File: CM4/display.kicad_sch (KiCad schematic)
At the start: 1 part, among them U10 4inch_RPi_LCD_(C)

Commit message: Started the "fun" of routing
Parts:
- U10: footprint Connector_PinSocket_2.54mm:PinSocket_2x13_P2.54mm_Vertical -> (none)
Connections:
- net +3.3 High Current: now also U10.17 (3.3V)
- net +5: now also U10.4 (5V)
- net GND: now also U10.14 (GND), U10.20 (GND), U10.25 (GND), U10.9 (GND)
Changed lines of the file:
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@@
 (kicad_sch (version 20210126) (generator eeschema)
   (paper "A4")
+  (wire (pts (xy 97.79 107.95) (xy 97.79 110.49))
+    (stroke (width 0) (type solid) (color 0 0 0 0))
+  )
+  (wire (pts (xy 97.79 113.03) (xy 97.79 114.935))
+    (stroke (width 0) (type solid) (color 0 0 0 0))
+  )
   (global_label "TP_CS" (shape input) (at 97.79 87.63 0)
     (effects (font (size 1.27 1.27)) (justify left))
@@
     )
   )
-  (global_label "+5" (shape input) (at 97.79 110.49 0)
+  (global_label "+3.3 High Current" (shape input) (at 97.79 107.95 0)
     (effects (font (size 1.27 1.27)) (justify left))
-    (property "Intersheet References" "${INTERSHEET_REFS}" (id 0) (at 102.985 110.4106 0)
+    (property "Intersheet References" "${INTERSHEET_REFS}" (id 0) (at 117.9226 107.8706 0)
       (effects (font (size 1.27 1.27)) (justify left) hide)
     )
   )
-  (global_label "+3.3 High Current" (shape input) (at 97.79 113.03 0)
+  (global_label "+5" (shape input) (at 97.79 113.03 0)
     (effects (font (size 1.27 1.27)) (justify left))
-    (property "Intersheet References" "${INTERSHEET_REFS}" (id 0) (at 117.9226 112.9506 0)
+    (property "Intersheet References" "${INTERSHEET_REFS}" (id 0) (at 102.985 112.9506 0)
       (effects (font (size 1.27 1.27)) (justify left) hide)
     )
   )
-  (symbol (lib_id "power:GND") (at 97.79 107.95 90) (unit 1)
+  (symbol (lib_id "power:GND") (at 78.74 121.285 0) (unit 1)
     (in_bom yes) (on_board yes)
-    (property "Reference" "#PWR0148" (id 0) (at 104.14 107.95 0)
+    (property "Reference" "#PWR0152" (id 0) (at 78.74 127.635 0)
       (effects (font (size 1.27 1.27)) hide)
     )
-    (property "Value" "GND" (id 1) (at 100.9651 108.3385 90)
+    (property "Value" "GND" (id 1) (at 78.3515 124.4601 90)
       (effects (font (size 1.27 1.27)) (justify right))
     )
-    (property "Footprint" "" (id 2) (at 97.79 107.95 0)
+    (property "Footprint" "" (id 2) (at 78.74 121.285 0)
       (effects (font (size 1.27 1.27)) hide)
     )
-    (property "Datasheet" "" (id 3) (at 97.79 107.95 0)
+    (property "Datasheet" "" (id 3) (at 78.74 121.285 0)
       (effects (font (size 1.27 1.27)) hide)
     )
     (pin "1")
   )
-  (symbol (lib_id "teensy:4inch_RPi_LCD_(C)") (at 85.725 101.6 0) (unit 1)
+  (symbol (lib_id "power:GND") (at 81.28 121.285 0) (unit 1)
     (in_bom yes) (on_board yes)
-    (property "Reference" "U10" (id 0) (at 86.5124 79.1676 0))
-    (property "Value" "4inch_RPi_LCD_(C)" (id 1) (at 86.5124 81.4663 0))
-    (property "Footprint" "Connector_PinSocket_2.54mm:PinSocket_2x13_P2.54mm_Vertical" (id 2) (at 85.09 45.085 0)
+    (property "Reference" "#PWR0151" (id 0) (at 81.28 127.635 0)
       (effects (font (size 1.27 1.27)) hide)
     )
-    (property "Datasheet" "" (id 3) (at 85.09 45.085 0)
+    (property "Value" "GND" (id 1) (at 80.8915 124.4601 90)
+      (effects (font (size 1.27 1.27)) (justify right))
+    )
+    (property "Footprint" "" (id 2) (at 81.28 121.285 0)
+      (effects (font (size 1.27 1.27)) hide)
+    )
+    (property "Datasheet" "" (id 3) (at 81.28 121.285 0)
       (effects (font (size 1.27 1.27)) hide)
     )
     (pin "1")
+  )
+  (symbol (lib_id "power:GND") (at 83.82 121.285 0) (unit 1)
+    (in_bom yes) (on_board yes)
+    (property "Reference" "#PWR0150" (id 0) (at 83.82 127.635 0)
+      (effects (font (size 1.27 1.27)) hide)
+    )
+    (property "Value" "GND" (id 1) (at 83.4315 124.4601 90)
+      (effects (font (size 1.27 1.27)) (justify right))
+    )
+    (property "Footprint" "" (id 2) (at 83.82 121.285 0)
+      (effects (font (size 1.27 1.27)) hide)
+    )
+    (property "Datasheet" "" (id 3) (at 83.82 121.285 0)
+      (effects (font (size 1.27 1.27)) hide)
+    )
+    (pin "1")
+  )
+  (symbol (lib_id "power:GND") (at 86.36 121.285 0) (unit 1)
+    (in_bom yes) (on_board yes)
+    (property "Reference" "#PWR0149" (id 0) (at 86.36 127.635 0)
+      (effects (font (size 1.27 1.27)) hide)
+    )
+    (property "Value" "GND" (id 1) (at 85.9715 124.4601 90)
+      (effects (font (size 1.27 1.27)) (justify right))
+    )
+    (property "Footprint" "" (id 2) (at 86.36 121.285 0)
+      (effects (font (size 1.27 1.27)) hide)
+    )
+    (property "Datasheet" "" (id 3) (at 86.36 121.285 0)
+      (effects (font (size 1.27 1.27)) hide)
+    )
+    (pin "1")
+  )
+  (symbol (lib_id "power:GND") (at 88.9 121.285 0) (unit 1)
+    (in_bom yes) (on_board yes)
+    (property "Reference" "#PWR0148" (id 0) (at 88.9 127.635 0)
+      (effects (font (size 1.27 1.27)) hide)
+    )
+    (property "Value" "GND" (id 1) (at 88.5115 124.4601 90)
+      (effects (font (size 1.27 1.27)) (justify right))
+    )
+    (property "Footprint" "" (id 2) (at 88.9 121.285 0)
+      (effects (font (size 1.27 1.27)) hide)
+    )
+    (property "Datasheet" "" (id 3) (at 88.9 121.285 0)
+      (effects (font (size 1.27 1.27)) hide)
+    )
+    (pin "1")
+  )
+  (symbol (lib_id "teensy:4inch_RPi_LCD_(C)") (at 25.4 105.41 0) (unit 1)
+    (in_bom yes) (on_board yes)
+    (property "Reference" "U10" (id 0) (at 85.09 80.4376 0))
+    (property "Value" "4inch_RPi_LCD_(C)" (id 1) (at 85.09 82.7363 0))
+    (property "Footprint" "" (id 2) (at 24.765 48.895 0)
+      (effects (font (size 1.27 1.27)) hide)
+    )
+    (property "Datasheet" "" (id 3) (at 24.765 48.895 0)
+      (effects (font (size 1.27 1.27)) hide)
+    )
+    (pin "1")
+    (pin "10")
     (pin "11")
+    (pin "12")
+    (pin "13")
+    (pin "14")
+    (pin "15")
+    (pin "16")
+    (pin "17")
     (pin "18")
     (pin "19")
     (pin "2")
+    (pin "20")
     (pin "21")
     (pin "22")
     (pin "23")
     (pin "24")
+    (pin "25")
     (pin "26")
+    (pin "3")
+    (pin "4")
+    (pin "5")
     (pin "6")
+    (pin "7")
+    (pin "8")
+    (pin "9")
   )
 )

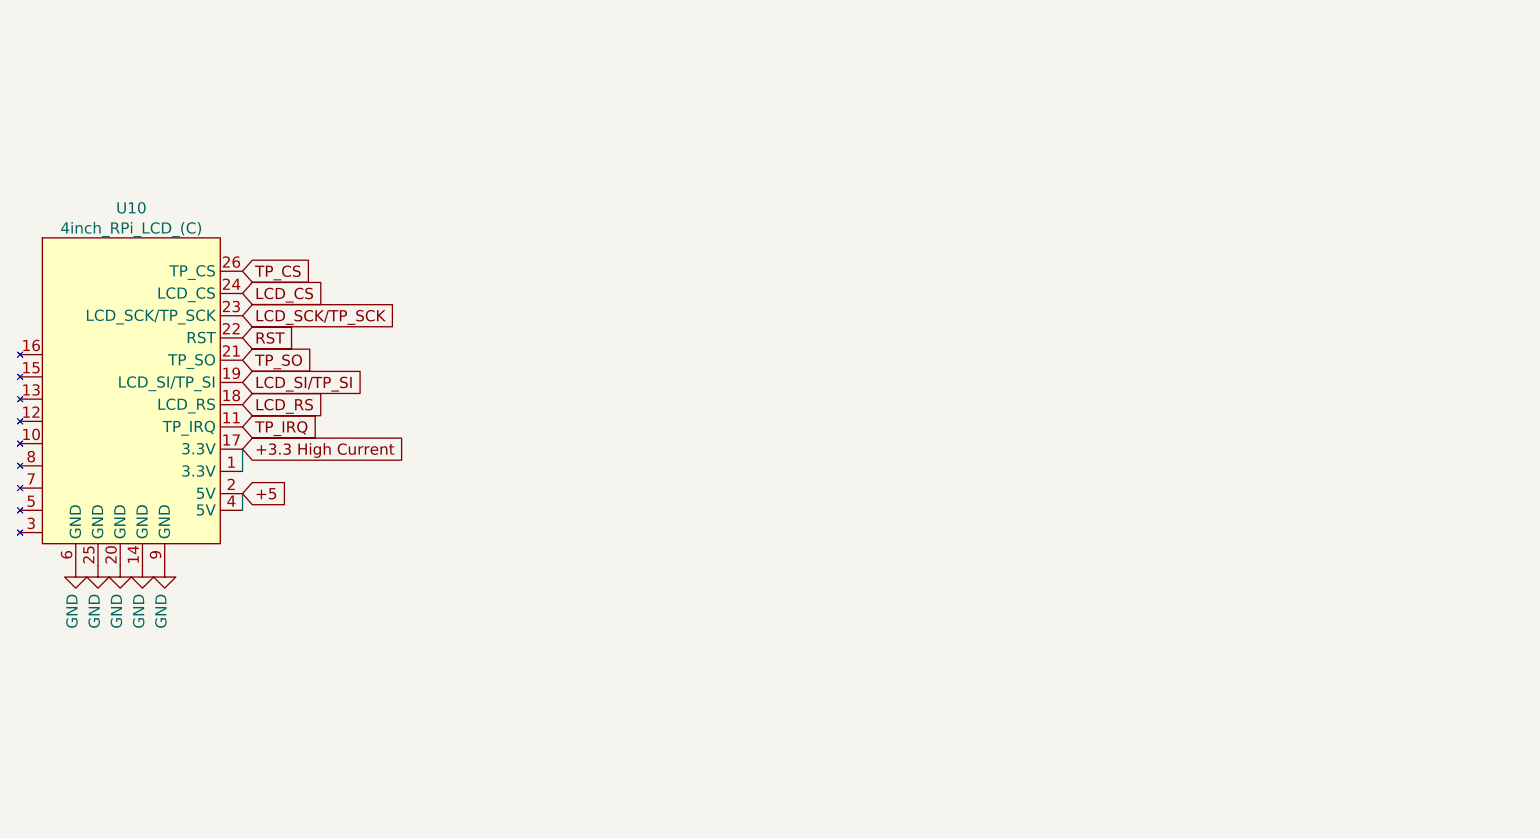
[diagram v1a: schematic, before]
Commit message: Bigone here we go
Whats gonna happon is im gonna get a 4 inch hdmi display and desolder the hdmi connector and add it to a ribbion cable and then add a connector to the pcb for hdmi to interface with that
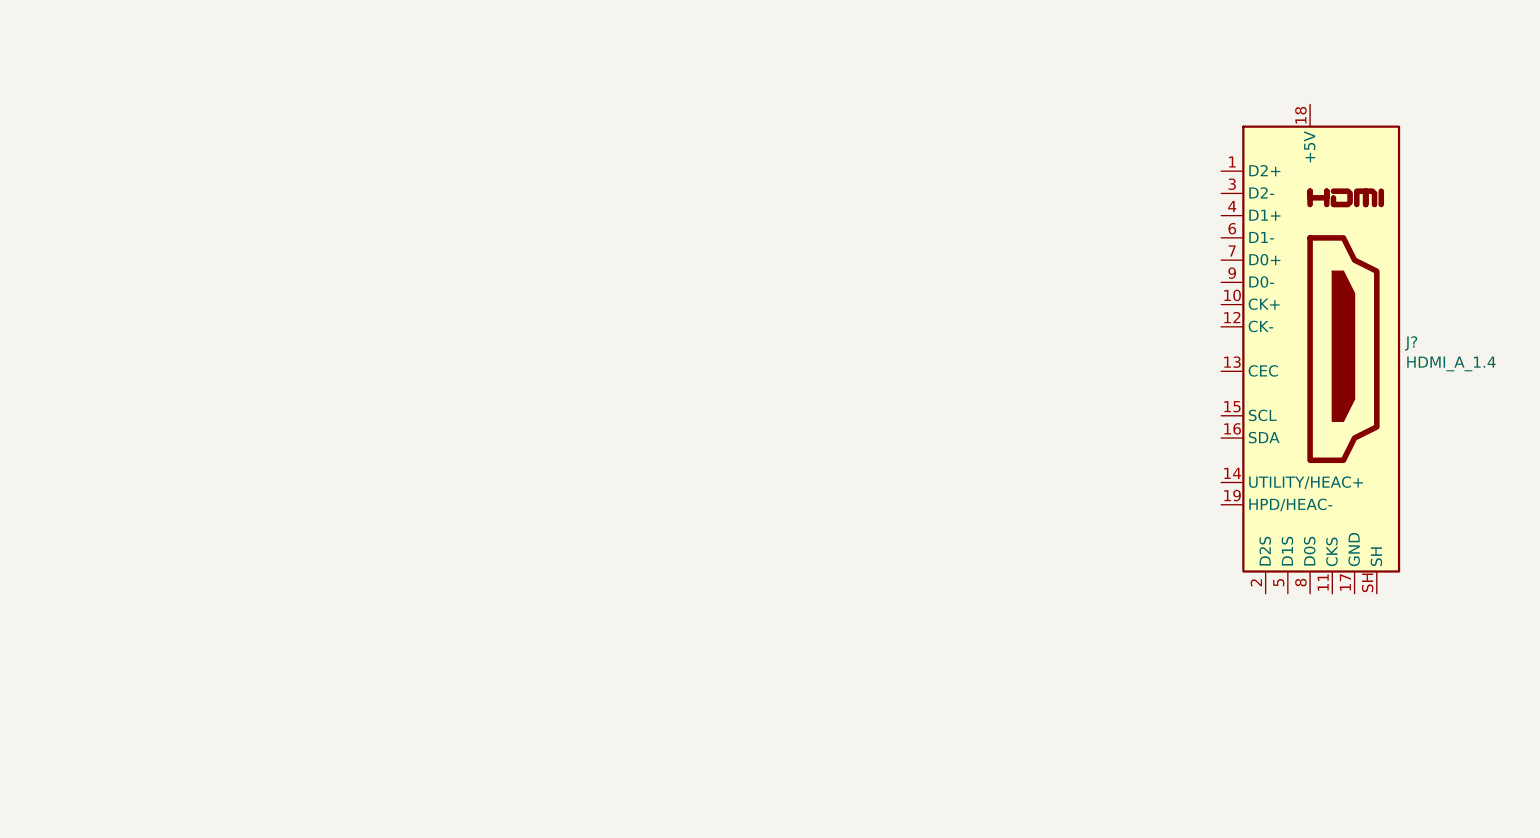
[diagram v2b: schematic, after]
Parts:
- removed U10: 4inch_RPi_LCD_(C), symbol teensy:4inch_RPi_LCD_(C)
- added J?: HDMI_A_1.4, symbol Connector:HDMI_A_1.4
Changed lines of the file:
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@@
 (kicad_sch (version 20210126) (generator eeschema)
   (paper "A4")
-  (wire (pts (xy 97.79 107.95) (xy 97.79 110.49))
-    (stroke (width 0) (type solid) (color 0 0 0 0))
-  )
-  (wire (pts (xy 97.79 113.03) (xy 97.79 114.935))
-    (stroke (width 0) (type solid) (color 0 0 0 0))
-  )
-  (global_label "TP_CS" (shape input) (at 97.79 87.63 0)
-    (effects (font (size 1.27 1.27)) (justify left))
-    (property "Intersheet References" "${INTERSHEET_REFS}" (id 0) (at 105.8879 87.5506 0)
-      (effects (font (size 1.27 1.27)) (justify left) hide)
+  (symbol (lib_id "Connector:HDMI_A_1.4") (at 219.71 96.52 0) (unit 1)
+    (in_bom yes) (on_board yes)
+    (property "Reference" "J?" (id 0) (at 230.6321 95.7591 0)
+      (effects (font (size 1.27 1.27)) (justify left))
     )
-  )
-  (global_label "LCD_CS" (shape input) (at 97.79 90.17 0)
-    (effects (font (size 1.27 1.27)) (justify left))
-    (property "Intersheet References" "${INTERSHEET_REFS}" (id 0) (at 107.2183 90.0906 0)
-      (effects (font (size 1.27 1.27)) (justify left) hide)
+    (property "Value" "HDMI_A_1.4" (id 1) (at 230.6321 98.0578 0)
+      (effects (font (size 1.27 1.27)) (justify left))
     )
-  )
-  (global_label "LCD_SCK{slash}TP_SCK" (shape input) (at 97.79 92.71 0)
-    (effects (font (size 1.27 1.27)) (justify left))
-    (property "Intersheet References" "${INTERSHEET_REFS}" (id 0) (at 116.7736 92.6306 0)
-      (effects (font (size 1.27 1.27)) (justify left) hide)
-    )
-  )
-  (global_label "RST" (shape input) (at 97.79 95.25 0)
-    (effects (font (size 1.27 1.27)) (justify left))
-    (property "Intersheet References" "${INTERSHEET_REFS}" (id 0) (at 103.6502 95.1706 0)
-      (effects (font (size 1.27 1.27)) (justify left) hide)
-    )
-  )
-  (global_label "TP_SO" (shape input) (at 97.79 97.79 0)
-    (effects (font (size 1.27 1.27)) (justify left))
-    (property "Intersheet References" "${INTERSHEET_REFS}" (id 0) (at 105.9483 97.7106 0)
-      (effects (font (size 1.27 1.27)) (justify left) hide)
-    )
-  )
-  (global_label "LCD_SI{slash}TP_SI" (shape input) (at 97.79 100.33 0)
-    (effects (font (size 1.27 1.27)) (justify left))
-    (property "Intersheet References" "${INTERSHEET_REFS}" (id 0) (at 112.9031 100.2506 0)
-      (effects (font (size 1.27 1.27)) (justify left) hide)
-    )
-  )
-  (global_label "LCD_RS" (shape input) (at 97.79 102.87 0)
-    (effects (font (size 1.27 1.27)) (justify left))
-    (property "Intersheet References" "${INTERSHEET_REFS}" (id 0) (at 107.2183 102.7906 0)
-      (effects (font (size 1.27 1.27)) (justify left) hide)
-    )
-  )
-  (global_label "TP_IRQ" (shape input) (at 97.79 105.41 0)
-    (effects (font (size 1.27 1.27)) (justify left))
-    (property "Intersheet References" "${INTERSHEET_REFS}" (id 0) (at 106.6136 105.3306 0)
-      (effects (font (size 1.27 1.27)) (justify left) hide)
-    )
-  )
-  (global_label "+3.3 High Current" (shape input) (at 97.79 107.95 0)
-    (effects (font (size 1.27 1.27)) (justify left))
-    (property "Intersheet References" "${INTERSHEET_REFS}" (id 0) (at 117.9226 107.8706 0)
-      (effects (font (size 1.27 1.27)) (justify left) hide)
-    )
-  )
-  (global_label "+5" (shape input) (at 97.79 113.03 0)
-    (effects (font (size 1.27 1.27)) (justify left))
-    (property "Intersheet References" "${INTERSHEET_REFS}" (id 0) (at 102.985 112.9506 0)
-      (effects (font (size 1.27 1.27)) (justify left) hide)
-    )
-  )
-  (symbol (lib_id "power:GND") (at 78.74 121.285 0) (unit 1)
-    (in_bom yes) (on_board yes)
-    (property "Reference" "#PWR0152" (id 0) (at 78.74 127.635 0)
+    (property "Footprint" "" (id 2) (at 220.345 96.52 0)
       (effects (font (size 1.27 1.27)) hide)
     )
-    (property "Value" "GND" (id 1) (at 78.3515 124.4601 90)
-      (effects (font (size 1.27 1.27)) (justify right))
-    )
-    (property "Footprint" "" (id 2) (at 78.74 121.285 0)
-      (effects (font (size 1.27 1.27)) hide)
-    )
-    (property "Datasheet" "" (id 3) (at 78.74 121.285 0)
-      (effects (font (size 1.27 1.27)) hide)
-    )
-    (pin "1")
-  )
-  (symbol (lib_id "power:GND") (at 81.28 121.285 0) (unit 1)
-    (in_bom yes) (on_board yes)
-    (property "Reference" "#PWR0151" (id 0) (at 81.28 127.635 0)
-      (effects (font (size 1.27 1.27)) hide)
-    )
-    (property "Value" "GND" (id 1) (at 80.8915 124.4601 90)
-      (effects (font (size 1.27 1.27)) (justify right))
-    )
-    (property "Footprint" "" (id 2) (at 81.28 121.285 0)
-      (effects (font (size 1.27 1.27)) hide)
-    )
-    (property "Datasheet" "" (id 3) (at 81.28 121.285 0)
-      (effects (font (size 1.27 1.27)) hide)
-    )
-    (pin "1")
-  )
-  (symbol (lib_id "power:GND") (at 83.82 121.285 0) (unit 1)
-    (in_bom yes) (on_board yes)
-    (property "Reference" "#PWR0150" (id 0) (at 83.82 127.635 0)
-      (effects (font (size 1.27 1.27)) hide)
-    )
-    (property "Value" "GND" (id 1) (at 83.4315 124.4601 90)
-      (effects (font (size 1.27 1.27)) (justify right))
-    )
-    (property "Footprint" "" (id 2) (at 83.82 121.285 0)
-      (effects (font (size 1.27 1.27)) hide)
-    )
-    (property "Datasheet" "" (id 3) (at 83.82 121.285 0)
-      (effects (font (size 1.27 1.27)) hide)
-    )
-    (pin "1")
-  )
-  (symbol (lib_id "power:GND") (at 86.36 121.285 0) (unit 1)
-    (in_bom yes) (on_board yes)
-    (property "Reference" "#PWR0149" (id 0) (at 86.36 127.635 0)
-      (effects (font (size 1.27 1.27)) hide)
-    )
-    (property "Value" "GND" (id 1) (at 85.9715 124.4601 90)
-      (effects (font (size 1.27 1.27)) (justify right))
-    )
-    (property "Footprint" "" (id 2) (at 86.36 121.285 0)
-      (effects (font (size 1.27 1.27)) hide)
-    )
-    (property "Datasheet" "" (id 3) (at 86.36 121.285 0)
-      (effects (font (size 1.27 1.27)) hide)
-    )
-    (pin "1")
-  )
-  (symbol (lib_id "power:GND") (at 88.9 121.285 0) (unit 1)
-    (in_bom yes) (on_board yes)
-    (property "Reference" "#PWR0148" (id 0) (at 88.9 127.635 0)
-      (effects (font (size 1.27 1.27)) hide)
-    )
-    (property "Value" "GND" (id 1) (at 88.5115 124.4601 90)
-      (effects (font (size 1.27 1.27)) (justify right))
-    )
-    (property "Footprint" "" (id 2) (at 88.9 121.285 0)
-      (effects (font (size 1.27 1.27)) hide)
-    )
-    (property "Datasheet" "" (id 3) (at 88.9 121.285 0)
-      (effects (font (size 1.27 1.27)) hide)
-    )
-    (pin "1")
-  )
-  (symbol (lib_id "teensy:4inch_RPi_LCD_(C)") (at 25.4 105.41 0) (unit 1)
-    (in_bom yes) (on_board yes)
-    (property "Reference" "U10" (id 0) (at 85.09 80.4376 0))
-    (property "Value" "4inch_RPi_LCD_(C)" (id 1) (at 85.09 82.7363 0))
-    (property "Footprint" "" (id 2) (at 24.765 48.895 0)
-      (effects (font (size 1.27 1.27)) hide)
-    )
-    (property "Datasheet" "" (id 3) (at 24.765 48.895 0)
+    (property "Datasheet" "https://en.wikipedia.org/wiki/HDMI" (id 3) (at 220.345 96.52 0)
       (effects (font (size 1.27 1.27)) hide)
     )
@@
     (pin "19")
     (pin "2")
-    (pin "20")
-    (pin "21")
-    (pin "22")
-    (pin "23")
-    (pin "24")
-    (pin "25")
-    (pin "26")
     (pin "3")
     (pin "4")
@@
     (pin "8")
     (pin "9")
+    (pin "SH")
   )
 )
